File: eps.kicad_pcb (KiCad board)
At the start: 2 copper layers, 95.9 x 90.2 mm, 181 parts, among them J1 PC104-8BIT, J2 PC104PTH, J3 PC104PTH, J4 PC104PTH, J5 PC104PTH, P1 3pin-DC-power, P2 3pin-DC-power, Q10 CSD17551Q3A, Q11 CSD17551Q3A, Q12 CSD17551Q3A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

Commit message: replaced 0.1inch jumpers with SMT jumpers, made board 4 layers
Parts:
- removed JP1A1, JP1B1: Conn_01x01, Socket_Strips:Socket_Strip_Straight_1x01_Pitch2.54mm
- removed JP2, JP3, JP4, JP5, JP6, JP8: Conn_01x02, Socket_Strips:Socket_Strip_Straight_1x02_Pitch2.54mm
- removed R52: 280k0, SFUSat-res:R_0603
- added R18: 0R, SFUSat-res:R_0603, F.Cu at (328.8, 169.1)
- added R19: DNP, SFUSat-res:R_0603, F.Cu at (354.8, 142.9)
- added R20: 0R, SFUSat-res:R_0603, F.Cu at (368.3, 129.4)
- added R21: DNP, SFUSat-res:R_0603, F.Cu at (359.7, 138.0)
- added R22: DNP, SFUSat-res:R_0603, F.Cu at (335.0, 160.8)
- added TP5: TEST, SFUSat:Measurement_Point_Round-SMD-Pad_Small, F.Cu at (314.9, 148.9)
- added TP8: TEST, SFUSat:Measurement_Point_Round-SMD-Pad_Small, F.Cu at (323.8, 134.2)
- added TP9: TEST, SFUSat:Measurement_Point_Round-SMD-Pad_Small, F.Cu at (311.1, 147.9)
- JP1: value Conn_01x03 -> Conn_01x02; footprint Socket_Strips:Socket_Strip_Straight_1x03_Pitch2.54mm -> Socket_Strips:Socket_Strip_Straight_1x02_Pitch2.54mm
- moved C33 203.8 mm to (364.7, 123.7)
- moved C31 178.8 mm to (335.0, 144.9)
- moved JP1 163.3 mm to (323.5, 125.3)
- moved TP11 161.5 mm to (336.5, 131.0)
- moved C35 153.0 mm to (319.5, 168.8)
- moved R54 150.0 mm to (363.9, 137.7)
- moved C23 149.7 mm to (351.4, 132.8)
- moved C49 147.5 mm to (349.3, 124.0)
- moved R50 146.2 mm to (341.0, 130.8)
- moved R7 142.2 mm to (360.6, 133.1)
- moved C25 141.0 mm to (341.4, 140.7)
- moved Q11 140.0 mm to (299.3, 135.6)
- moved R49 138.8 mm to (359.0, 142.7)
- moved R44 137.8 mm to (371.7, 129.4)
- moved R14 134.7 mm to (365.0, 127.9)
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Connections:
- C48 pad 2: /BMS/VBAT+ -> /pack+
- C51 pad 1: /BMS/VBAT+ -> /pack+
- D2 pad 1: /BMS/VBAT+ -> /pack+
- D4 pad 2: /BMS/VBAT+ -> /pack+
- JP1 pad 1: Net-(JP1-Pad1) -> /BMS/VIN+
- JP1 pad 2: GND -> Net-(C17-Pad1)
- Q5 pad 5: /BMS/VIN -> /BMS/VIN+
- Q5 pad 6: /BMS/VIN -> /BMS/VIN+
- Q5 pad 7: /BMS/VIN -> /BMS/VIN+
- Q5 pad 8: /BMS/VIN -> /BMS/VIN+
- R1 pad 1: /BMS/VIN -> /BMS/VIN+
- R17 pad 2: Net-(JP8-Pad2) -> Net-(C28-Pad1)
- R2 pad 1: /BMS/VIN -> /BMS/VIN+
- R31 pad 2: /BMS/VIN -> /BMS/VIN+
- R36 pad 2: Net-(JP1-Pad3) -> Net-(R36-Pad2)
- R38 pad 2: Net-(JP1-Pad1) -> Net-(R38-Pad2)
- R39 pad 1: Net-(JP1-Pad1) -> Net-(R38-Pad2)
- R41 pad 1: Net-(JP1-Pad3) -> Net-(R36-Pad2)
- R41 pad 2: Net-(JP1-Pad1) -> Net-(R38-Pad2)
- R50 pad 2: /BMS/VBAT+ -> /pack+
- R54 pad 1: /BMS/VBAT+ -> /pack+
- SW3 pad NC: /BMS/VIN -> /BMS/VIN+
- U4 pad 1: GND -> GNDPWR
- U4 pad 2: GND -> GNDPWR
- U5 pad 1: Net-(U5-Pad1) -> (no net)
- U5 pad 2: /PowerDistributionDeploymentControl/1.6A -> (no net)
- U5 pad 3: /PowerDistributionDeploymentControl/1.6A -> (no net)
- U5 pad 4: /+z_rail -> (no net)
- U5 pad 5: /+z_rail -> (no net)
- U5 pad 6: GND -> (no net)
- U6 pad 1: Net-(U6-Pad1) -> (no net)
- U6 pad 2: /PowerDistributionDeploymentControl/1.6A -> (no net)
- U6 pad 3: /PowerDistributionDeploymentControl/1.6A -> (no net)
- U6 pad 4: /-z_rail -> (no net)
- U6 pad 5: /-z_rail -> (no net)
- U6 pad 6: GND -> (no net)
- U7 pad 14: Net-(JP1-Pad1) -> Net-(R38-Pad2)
- U7 pad 15: Net-(JP1-Pad3) -> Net-(R36-Pad2)
- U8 pad 4: Net-(U6-Pad1) -> Net-(U6-PadC2)
- U8 pad 6: Net-(U5-Pad1) -> Net-(U5-PadC2)
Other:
- copper layers 2 -> 4
- board text added: "Stackup: ------------- Copper 1 35 um ============= Dielectric 1-2 0.175 mm (e.g. 1x Prepreg 7628 AT05 47% Resin) TG130 dk 4.29 ------------- Copper 2 35 um ============= Dielectric 2-3 1.13 mm (6x 7628M 43% Resin) TG150 dk 3.96 ------------- Copper 3 35 um ============= Dielectric 3-4 0.175 mm (e.g. 1x Prepreg 7628 AT05 47% Resin) TG130 dk 4.29 ------------- Copper 4 35 um"

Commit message: Started laying out the components, spacings and positions are temporary most are just placed relative to their locations in the schematic
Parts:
- removed JP1: Conn_01x02, Socket_Strips:Socket_Strip_Straight_1x02_Pitch2.54mm
- removed JP7: Conn_01x03, Socket_Strips:Socket_Strip_Straight_1x03_Pitch2.54mm
- removed U8: CD4555B, SFUSat:CD4555BPWR
- R8: value 100.0 kOhm -> 100k
- moved TP20 220.1 mm to (503.1, 168.0)
- moved D4 198.4 mm to (514.6, 163.6)
- moved TP12 194.8 mm to (500.0, 158.5)
- moved C51 177.0 mm to (511.4, 163.6)
- moved C48 176.1 mm to (501.8, 162.9)
- moved D5 172.8 mm to (443.3, 246.1), turned to 270 degrees
- moved TP18 171.7 mm to (500.6, 168.0)
- moved U9 168.8 mm to (445.4, 249.9), turned to 180 degrees
- moved D2 167.5 mm to (440.9, 246.1), turned to 270 degrees
- moved TP9 167.3 mm to (446.0, 246.8)
- moved R50 163.5 mm to (501.6, 161.0)
- moved C56 162.5 mm to (435.8, 202.3), turned to 90 degrees
- moved TP24 161.5 mm to (475.2, 169.3)
- moved C55 159.0 mm to (442.2, 202.3)
- moved C42 156.2 mm to (452.9, 227.1)
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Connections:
- C33 pad 1: Net-(C29-Pad1) -> Net-(C33-Pad1)
- C34 pad 1: Net-(C29-Pad1) -> Net-(C33-Pad1)
- L1 pad 1: Net-(C29-Pad1) -> Net-(C33-Pad1)
- Q10 pad 5: Net-(C29-Pad1) -> Net-(C33-Pad1)
- Q10 pad 6: Net-(C29-Pad1) -> Net-(C33-Pad1)
- Q10 pad 7: Net-(C29-Pad1) -> Net-(C33-Pad1)
- Q10 pad 8: Net-(C29-Pad1) -> Net-(C33-Pad1)
- Q9 pad 1: Net-(C29-Pad1) -> Net-(C33-Pad1)
- Q9 pad 2: Net-(C29-Pad1) -> Net-(C33-Pad1)
- Q9 pad 3: Net-(C29-Pad1) -> Net-(C33-Pad1)
- TP2 pad 1: Net-(C29-Pad1) -> Net-(C33-Pad1)
- U7 pad 32: Net-(C29-Pad1) -> Net-(C33-Pad1)
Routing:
- net Net-(C2-Pad1): track 0.00 -> 15.3 mm

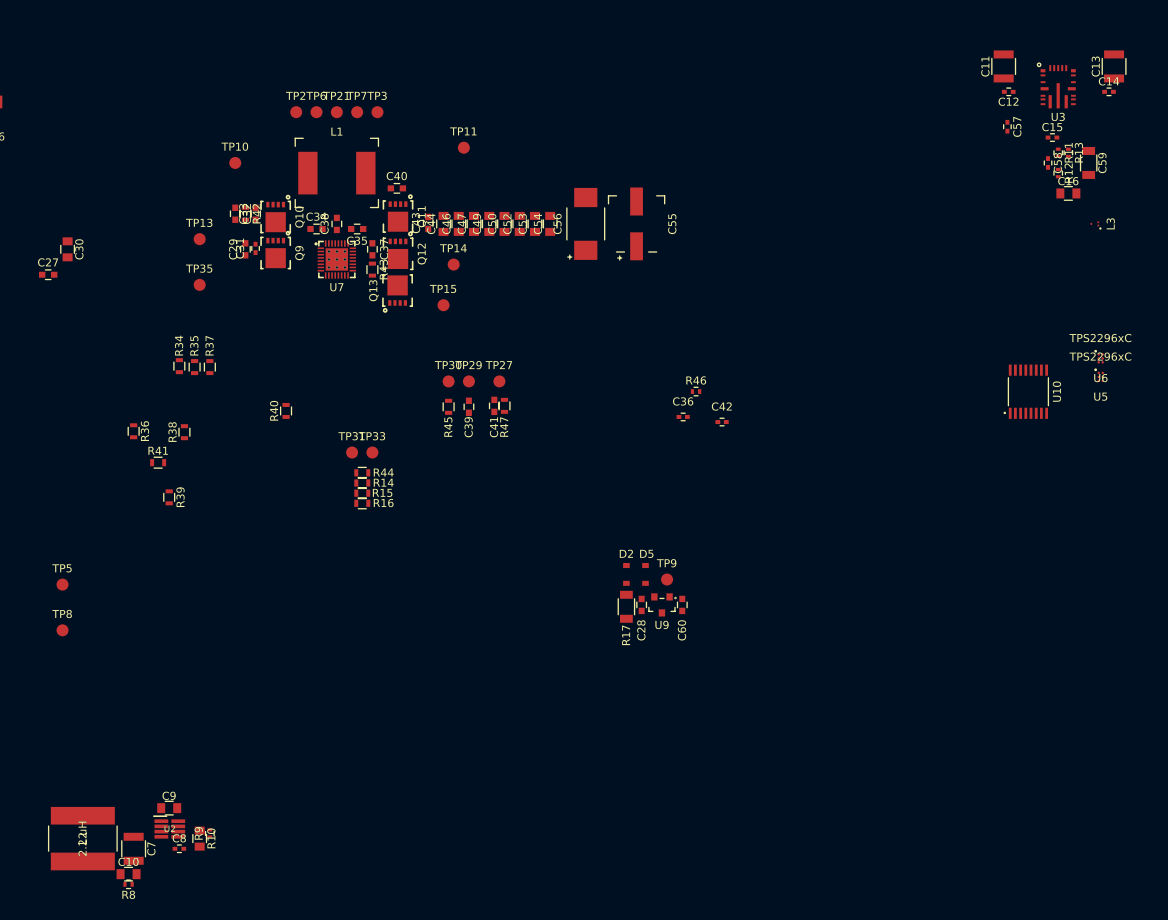
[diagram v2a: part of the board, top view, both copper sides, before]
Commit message: fixed demultiplexer
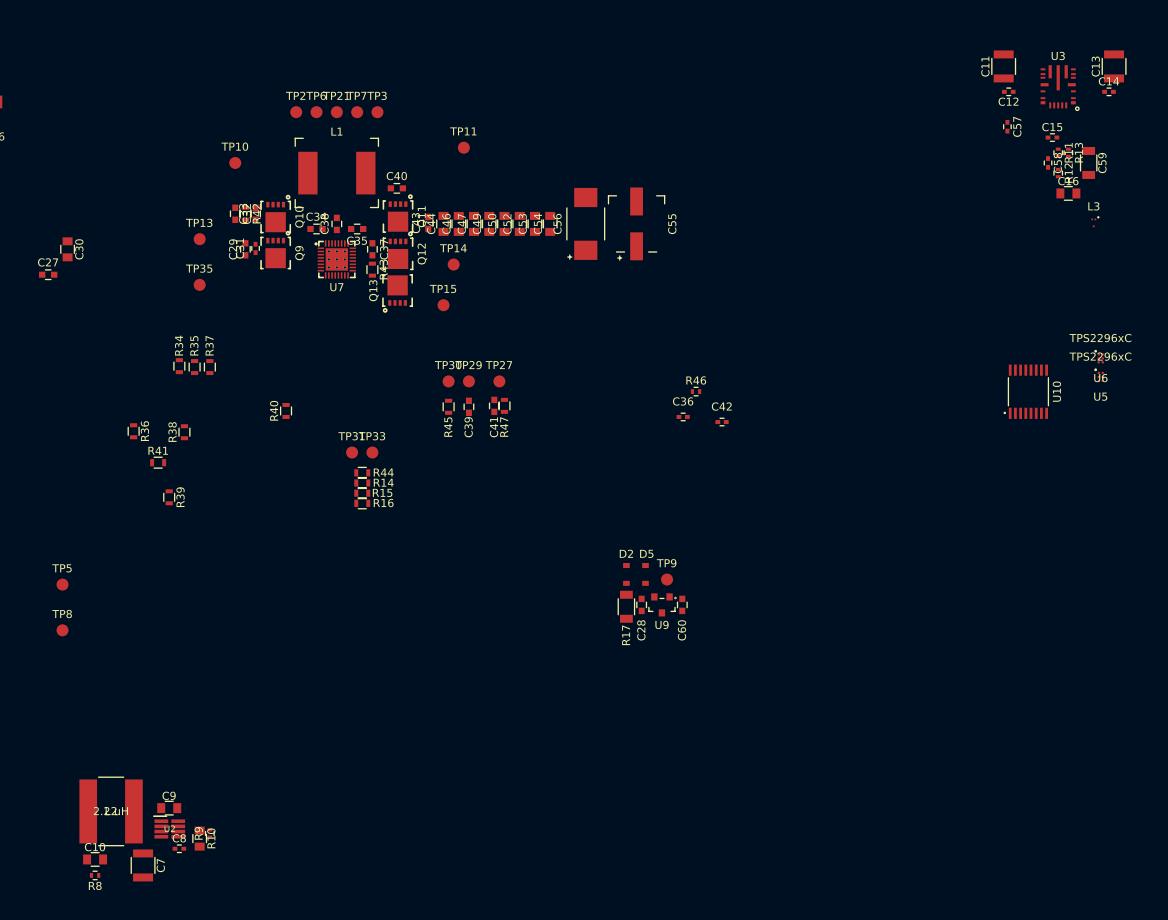
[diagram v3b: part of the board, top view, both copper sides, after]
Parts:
- moved L2 4.90 mm to (376.5, 275.8), turned to 0 degrees
- moved C10 4.57 mm to (374.5, 281.8)
- moved R8 4.33 mm to (374.5, 283.8)
- moved C7 2.40 mm to (380.5, 282.5)
- turned L3 to 180 degrees
- turned U3 to 180 degrees

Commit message: Fixed TPS22964xC IC Pins
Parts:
- added JP1: Conn_01x02, Socket_Strips:Socket_Strip_Straight_1x02_Pitch2.54mm, F.Cu at (169.8, 144.3)
- added JP7: Conn_01x03, Socket_Strips:Socket_Strip_Straight_1x03_Pitch2.54mm, F.Cu at (145.1, 145.3)
- C10, C9: footprint Capacitors_SMD:C_0805 -> SFUSat-cap:C_0805
- C7: footprint Capacitors_SMD:C_1210 -> SFUSat-cap:C_1210
- moved C11 224.2 mm to (333.6, 345.2)
- moved C13 224.2 mm to (347.4, 345.2)
- moved C14 224.2 mm to (346.8, 348.4)
- moved C15 224.2 mm to (339.7, 354.1)
- moved C16 224.2 mm to (341.7, 361.1)
- moved C57 224.2 mm to (334.1, 352.7)
- moved C58 224.2 mm to (339.2, 357.2)
- moved C59 224.2 mm to (344.3, 357.2)
- moved R11 224.2 mm to (340.5, 356.0)
- moved R13 224.2 mm to (341.7, 356.0)
- moved U3 224.2 mm to (340.5, 347.7)
- moved C12 224.2 mm to (334.3, 348.4)
- moved R12 224.2 mm to (340.5, 358.5)
- moved L3 202.5 mm to (369.1, 357.4), turned to 270 degrees
- moved U5 188.0 mm to (330.6, 302.6), turned to 180 degrees
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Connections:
- U10 pad 2: Net-(U10-Pad2) -> /DPL_SEL
- U10 pad 3: Net-(U10-Pad3) -> GND
- U5 pad 1: (no net) -> /+z_rail
- U5 pad 2: (no net) -> /+z_rail
- U5 pad 3: (no net) -> GND
- U5 pad 4: (no net) -> Net-(U10-Pad4)
- U5 pad 5: (no net) -> /PowerDistributionDeploymentControl/1.6A
- U5 pad 6: (no net) -> /PowerDistributionDeploymentControl/1.6A
- U6 pad 1: (no net) -> /-z_rail
- U6 pad 2: (no net) -> /-z_rail
- U6 pad 3: (no net) -> GND
- U6 pad 4: (no net) -> Net-(U10-Pad5)
- U6 pad 5: (no net) -> /PowerDistributionDeploymentControl/1.6A
- U6 pad 6: (no net) -> /PowerDistributionDeploymentControl/1.6A

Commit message: Placed the Power Distribution Circuits on the PCB
Includes traces rated for 2A.
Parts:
- moved C16 378.2 mm to (121.8, 53.3), turned to 180 degrees
- moved C15 371.1 mm to (124.9, 51.5), turned to 180 degrees
- moved C14 370.0 mm to (121.2, 55.1), turned to 180 degrees
- moved R12 366.7 mm to (144.3, 48.7), turned to 0 degrees
- moved C13 365.2 mm to (121.8, 58.1), turned to 270 degrees
- moved C58 363.5 mm to (144.9, 50.0), turned to 180 degrees
- moved R11 362.5 mm to (144.2, 51.2), turned to 180 degrees
- moved U3 361.7 mm to (127.6, 55.3), turned to 0 degrees
- moved C57 361.2 mm to (124.0, 59.0)
- moved L3 360.1 mm to (164.9, 60.8)
- moved C59 359.7 mm to (143.7, 58.6), turned to 180 degrees
- moved C12 356.5 mm to (133.3, 53.9), turned to 0 degrees
- moved R13 354.9 mm to (144.9, 60.7), turned to 180 degrees
- moved C11 351.3 mm to (132.7, 57.1), turned to 270 degrees
- moved C7 349.0 mm to (131.2, 67.2)
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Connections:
- SW1 pad COM: /1.6A_Regulator_PDB/1.6A -> /Vin_Solar
- SW1 pad NC: /PowerDistributionDeploymentControl/1.6A -> /BMS/VIN+
- SW3 pad COM: /Vin_Solar -> /1.6A_Regulator_PDB/1.6A
- SW3 pad NC: /BMS/VIN+ -> /PowerDistributionDeploymentControl/1.6A
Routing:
- net /return: track 0.00 -> 64.0 mm
- net /PowerDistributionDeploymentControl/1.6A: track 0.00 -> 51.1 mm
- net GND: track 0.00 -> 39.7 mm, vias 0 -> 24
- net /Vin_Solar: track 0.00 -> 39.1 mm
- net Net-(C57-Pad2): track 0.00 -> 34.8 mm
- net /1.6A_Regulator_PDB/1.6A: track 0.00 -> 33.6 mm
- net Net-(C58-Pad2): track 0.00 -> 22.9 mm
- net Net-(C9-Pad1): track 0.00 -> 20.1 mm
- net /VSYS_RETURN: track 0.00 -> 15.9 mm, vias 0 -> 8
- net /3V3: track 0.00 -> 11.0 mm, vias 0 -> 6
- net Net-(C57-Pad1): track 0.00 -> 7.54 mm
- net Net-(R10-Pad1): track 0.00 -> 4.14 mm
- net Net-(C16-Pad1): track 0.00 -> 2.87 mm
- net Net-(SW3-PadNO): track 0.00 -> 2.30 mm, vias 0 -> 1
- net Net-(R8-Pad1): track 0.00 -> 2.03 mm
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- added copper zone on PWR.Cu, net /3V3
- added copper zone on PWR.Cu, net /VSYS_RETURN

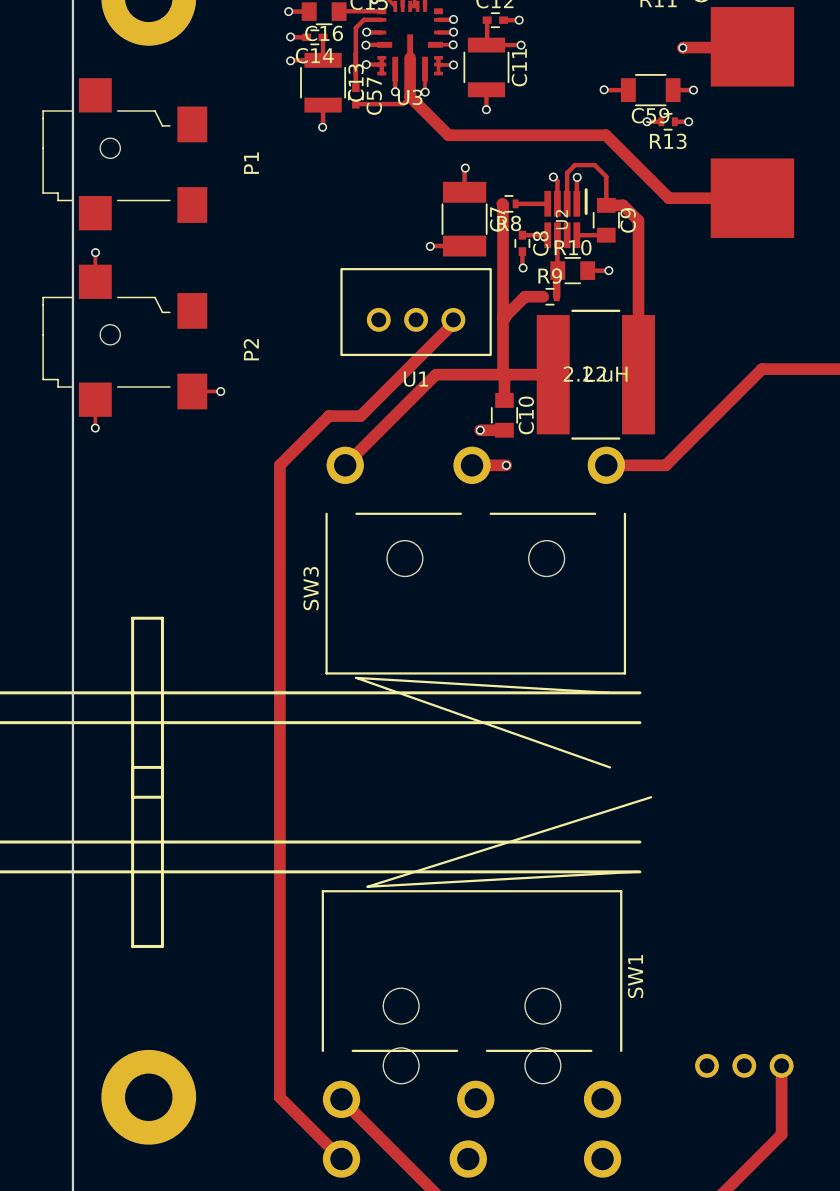
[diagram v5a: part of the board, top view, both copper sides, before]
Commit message: Layed Out the Limit Switch Connections
Inputs from limit switches for the BMS have been created and traced out.
Only implementation left is the BMS then connections from the BUS
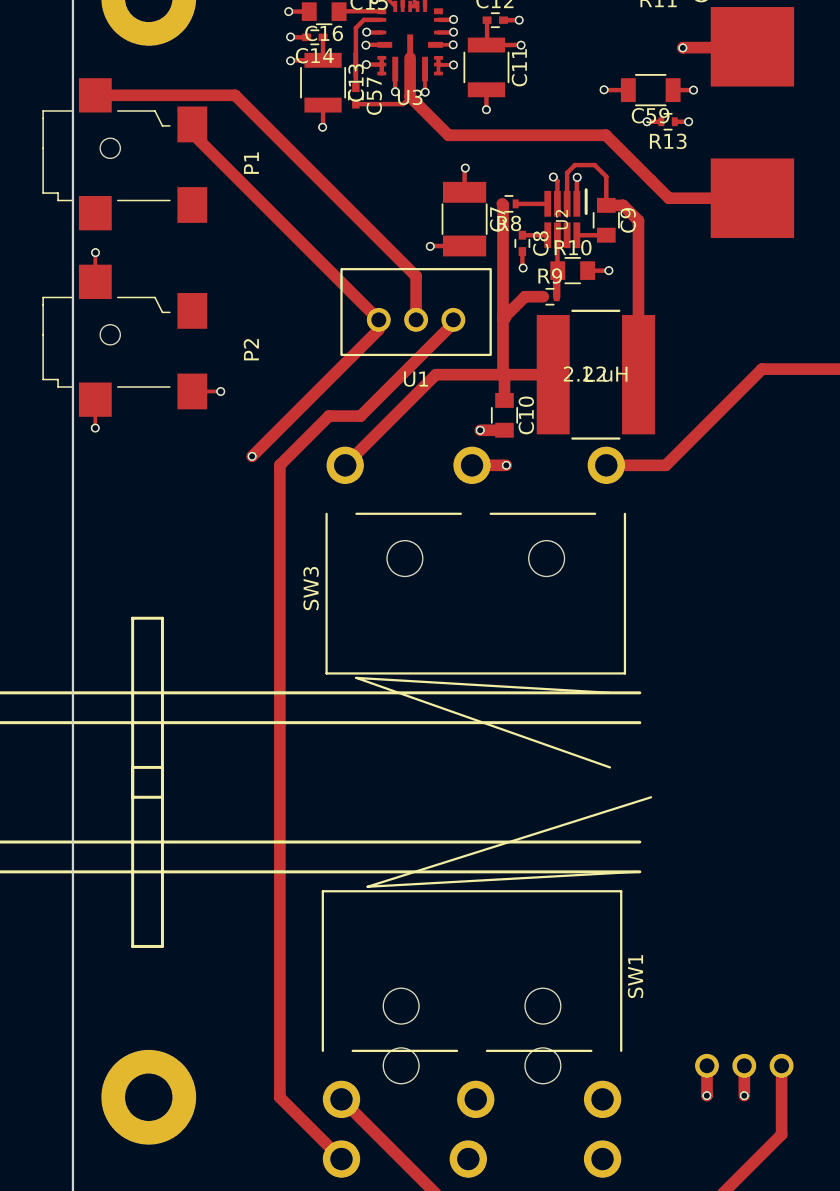
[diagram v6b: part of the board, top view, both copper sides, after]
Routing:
- net /pack+: track 0.60 -> 30.9 mm, vias 0 -> 1
- net /pack-: track 0.00 -> 29.4 mm
- net GNDPWR: track 0.00 -> 4.00 mm, vias 0 -> 2
- added copper zone on PWR.Cu, net /pack+
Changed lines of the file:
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@@
   (general
     (links 451)
-    (no_connects 401)
-    (area 104.924999 44.754999 200.965001 135.075001)
+    (no_connects 399)
+    (area 83.114286 22.899999 518.15 256.185)
     (thickness 1.6)
     (drawings 46)
-    (tracks 216)
+    (tracks 228)
     (zones 0)
     (modules 179)
@@
   (via (at 114.906 78.8025) (size 0.6) (drill 0.4) (layers F.Cu B.Cu) (net 42))
   (segment (start 114.9035 78.8) (end 114.906 78.8025) (width 0.25) (layer F.Cu) (net 42))
+  (segment (start 147.5 124) (end 147.5 125.99) (width 0.781) (layer F.Cu) (net 44))
+  (via (at 147.49 126) (size 0.6) (drill 0.4) (layers F.Cu B.Cu) (net 44))
+  (segment (start 147.5 125.99) (end 147.49 126) (width 0.781) (layer F.Cu) (net 44))
+  (segment (start 150 124) (end 150 126) (width 0.781) (layer F.Cu) (net 44))
+  (via (at 150 126) (size 0.6) (drill 0.4) (layers F.Cu B.Cu) (net 44))
   (segment (start 318.995 215.055) (end 324.06 215.055) (width 0.25) (layer F.Cu) (net 45))
   (segment (start 324.06 215.055) (end 324.075 215.04) (width 0.25) (layer F.Cu) (net 45))
@@
   (segment (start 137.425 72.45) (end 137.425 70.7) (width 0.5) (layer F.Cu) (net 97))
   (segment (start 137.475 70.65) (end 137.475 68.329) (width 0.3) (layer F.Cu) (net 97))
+  (segment (start 125.5 74) (end 125.5 74.66) (width 0.781) (layer F.Cu) (net 98))
+  (segment (start 125.5 74.66) (end 117.01 83.15) (width 0.781) (layer F.Cu) (net 98))
+  (via (at 117.01 83.15) (size 0.6) (drill 0.4) (layers F.Cu B.Cu) (net 98))
   (segment (start 113 60.9) (end 113 61.5) (width 0.781) (layer F.Cu) (net 98))
+  (segment (start 113 61.5) (end 125.5 74) (width 0.781) (layer F.Cu) (net 98))
   (segment (start 130.5 74) (end 130.5 74.23) (width 0.781) (layer F.Cu) (net 99))
   (segment (start 130.5 74.23) (end 124.28 80.45) (width 0.781) (layer F.Cu) (net 99))
@@
   (segment (start 118.87 83.74) (end 118.87 126.12) (width 0.781) (layer F.Cu) (net 99))
   (segment (start 118.87 126.12) (end 123 130.25) (width 0.781) (layer F.Cu) (net 99))
+  (segment (start 128 74) (end 128 71.08) (width 0.781) (layer F.Cu) (net 100))
+  (segment (start 128 71.08) (end 115.87 58.95) (width 0.781) (layer F.Cu) (net 100))
+  (segment (start 115.87 58.95) (end 106.5 58.95) (width 0.781) (layer F.Cu) (net 100))
   (segment (start 152.5 124) (end 152.5 128.61) (width 0.781) (layer F.Cu) (net 103))
   (segment (start 130.16 133.41) (end 123 126.25) (width 0.781) (layer F.Cu) (net 103))
@@
   (segment (start 146.58 49.98) (end 146.6 50) (width 0.5) (layer F.Cu) (net 107))
   (via (at 146.6 50) (size 0.6) (drill 0.4) (layers F.Cu B.Cu) (net 107))
-  (segment (start 140.75 83.75) (end 144.74 83.75) (width 0.781) (layer F.Cu) (net 117) (status 400000))
+  (segment (start 140.75 83.75) (end 144.74 83.75) (width 0.781) (layer F.Cu) (net 117))
   (segment (start 180.65 66.41) (end 182.16 66.41) (width 0.781) (layer F.Cu) (net 117))
   (segment (start 177.8 69.26) (end 180.65 66.41) (width 0.781) (layer F.Cu) (net 117))
@@
       )
     )
+  )
+  (zone (net 98) (net_name /pack+) (layer PWR.Cu) (hatch none 0.508)
+    (connect_pads (clearance 0.508))
+    (min_thickness 0.254)
+    (fill yes (arc_segments 16) (thermal_gap 0.508) (thermal_bridge_width 0.508))
+    (polygon
+      (pts
+        (xy 106.4 82.14) (xy 106.4 118.02) (xy 130.14 118.02) (xy 130.14 82.09) (xy 106.4 82.09)
+      )
+    )
